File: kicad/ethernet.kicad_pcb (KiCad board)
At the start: 2 copper layers, 2 parts, among them J1 RJ45_Abracon_ARJP11A-MASA-B-A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, U1 MSP432E401Y

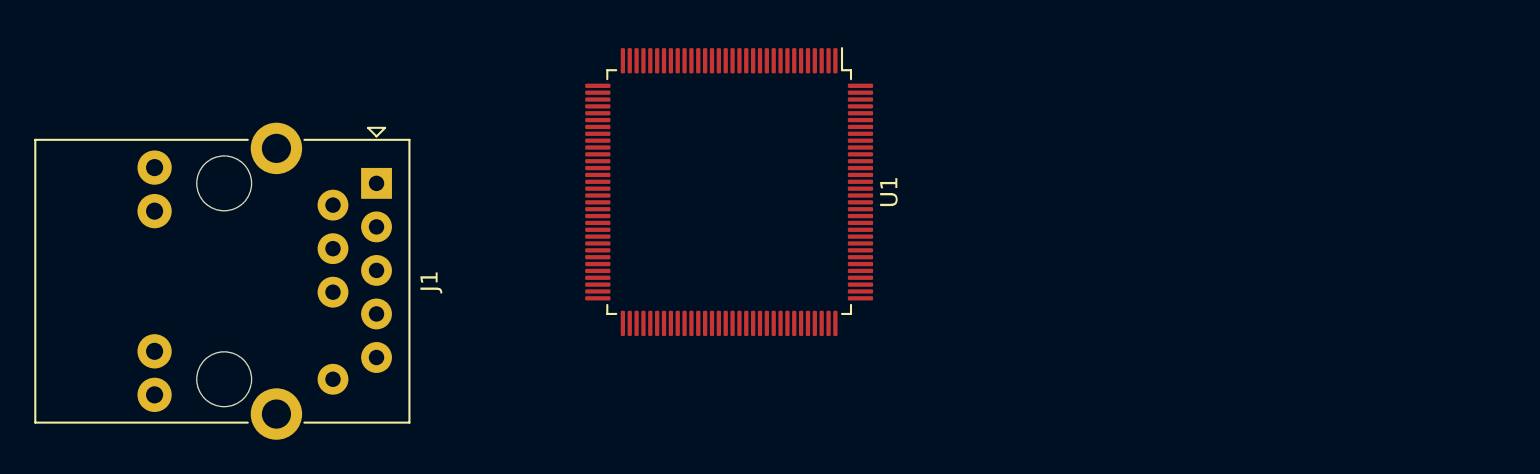
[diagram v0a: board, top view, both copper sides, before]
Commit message: working on ethernet board
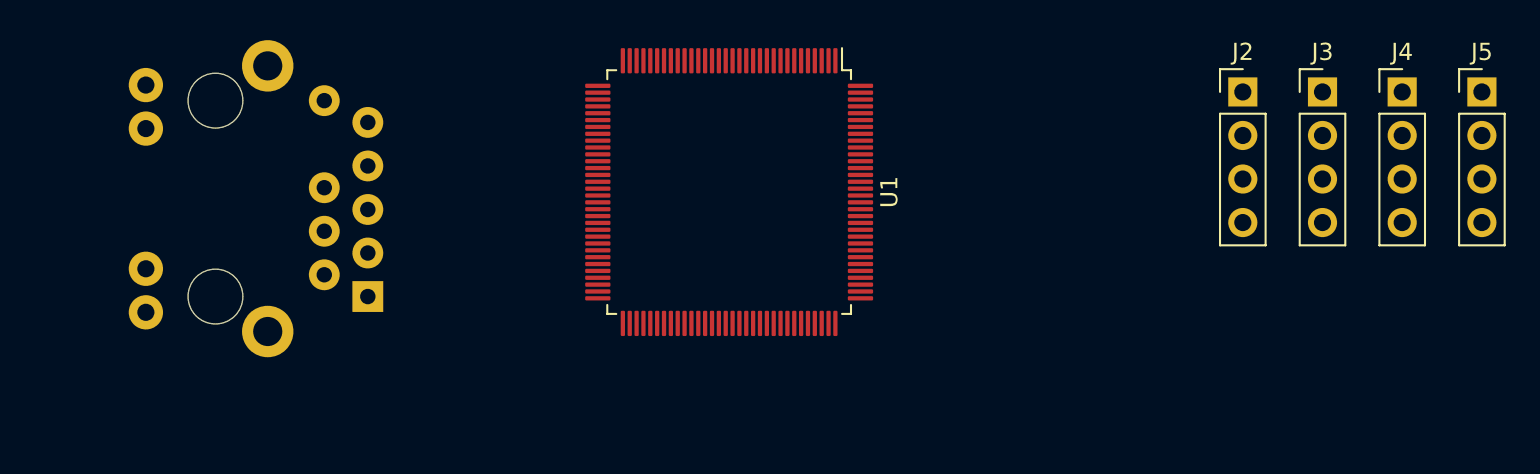
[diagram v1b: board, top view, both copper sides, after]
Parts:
- added J2: Conn_01x04_Male, Connector_PinHeader_2.54mm:PinHeader_1x04_P2.54mm_Vertical, F.Cu at (91.7, 32.0)
- added J3: Conn_01x04_Male, Connector_PinHeader_2.54mm:PinHeader_1x04_P2.54mm_Vertical, F.Cu at (96.3, 32.0)
- added J4: Conn_01x04_Male, Connector_PinHeader_2.54mm:PinHeader_1x04_P2.54mm_Vertical, F.Cu at (101.0, 32.0)
- added J5: Conn_01x04_Male, Connector_PinHeader_2.54mm:PinHeader_1x04_P2.54mm_Vertical, F.Cu at (105.6, 32.0)
- J1: moved to B.Cu
- moved J1 6.62 mm to (40.6, 43.9), turned to 90 degrees
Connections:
- J1 pad 7: Net-(J1-Pad7) -> GND
- U1 pad 10: Net-(U1-Pad10) -> GND
- U1 pad 114: Net-(U1-Pad114) -> GND
- U1 pad 17: Net-(U1-Pad114) -> GND
- U1 pad 48: Net-(U1-Pad114) -> GND
- U1 pad 55: Net-(U1-Pad114) -> GND
- U1 pad 58: Net-(U1-Pad114) -> GND
- U1 pad 80: Net-(U1-Pad114) -> GND

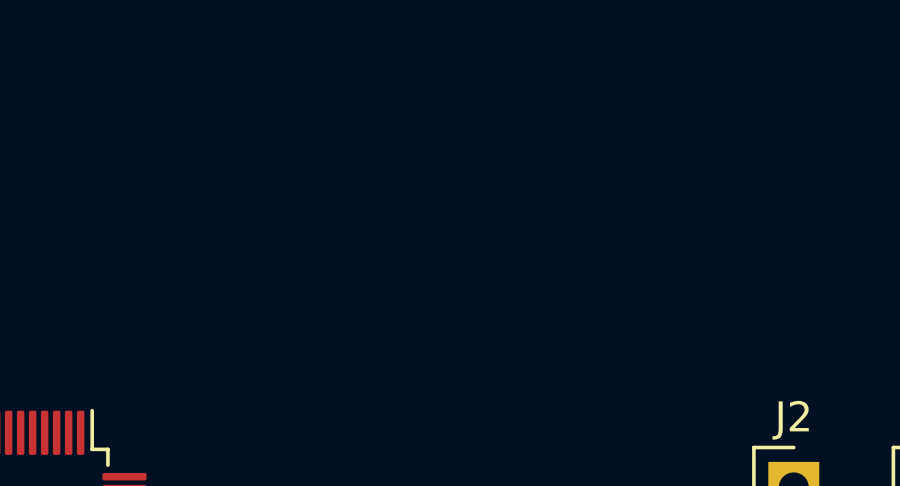
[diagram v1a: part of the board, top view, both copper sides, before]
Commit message: add QSPI flash to ethernet board
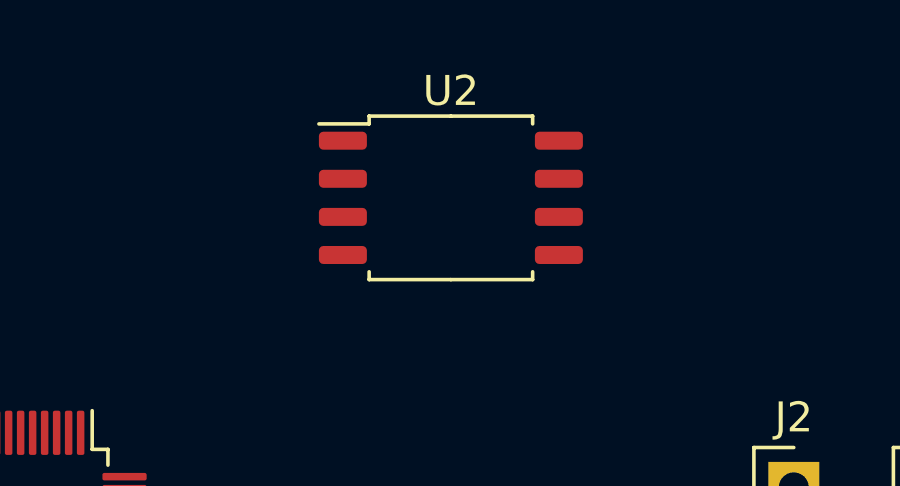
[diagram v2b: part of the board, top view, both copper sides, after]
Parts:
- added U2: W25Q32JVSS, Package_SO:SOIC-8_5.23x5.23mm_P1.27mm, F.Cu at (80.3, 22.4)
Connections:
- J1 pad 4: Net-(J1-Pad4) -> +3V3
- J1 pad 5: Net-(J1-Pad5) -> +3V3

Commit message: updating board
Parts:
- removed J2, J3, J4, J5: Conn_01x04_Male, Connector_PinHeader_2.54mm:PinHeader_1x04_P2.54mm_Vertical
- removed U2: W25Q32JVSS, Package_SO:SOIC-8_5.23x5.23mm_P1.27mm
- added R1: 49.9, Resistor_SMD:R_0805_2012Metric, F.Cu at (45.5, 32.5)
- added R2: 49.9, Resistor_SMD:R_0805_2012Metric, F.Cu at (49.0, 30.5)
- added R3: 49.9, Resistor_SMD:R_0805_2012Metric, F.Cu at (45.5, 29.0)
- added R4: 49.9, Resistor_SMD:R_0805_2012Metric, F.Cu at (49.0, 27.0)
- J1: moved to F.Cu
- U1: value MSP432E401Y -> TM4C1294NCPDTI3; footprint Package_QFP:LQFP-128_14x14mm_P0.4mm -> Package_QFP:TQFP-128_14x14mm_P0.4mm
- moved J1 17.2 mm to (39.0, 26.8), turned to -90 degrees
- moved U1 9.40 mm to (66.5, 29.8)
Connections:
- J1 pad 10: Net-(J1-Pad10) -> unconnected-(J1-Pad10)
- J1 pad 11: Net-(J1-Pad11) -> unconnected-(J1-Pad11)
- J1 pad 12: Net-(J1-Pad12) -> unconnected-(J1-Pad12)
- J1 pad 13: Net-(J1-Pad13) -> unconnected-(J1-Pad13)
- J1 pad 14: Net-(J1-Pad14) -> unconnected-(J1-Pad14)
- J1 pad 15: Net-(J1-Pad15) -> unconnected-(J1-Pad15)
- J1 pad 9: Net-(J1-Pad9) -> unconnected-(J1-Pad9)
- U1 pad 1: Net-(U1-Pad1) -> unconnected-(U1-Pad1)
- U1 pad 100: Net-(U1-Pad100) -> unconnected-(U1-Pad100)
- U1 pad 101: Net-(U1-Pad101) -> unconnected-(U1-Pad101)
- U1 pad 102: Net-(U1-Pad102) -> unconnected-(U1-Pad102)
- U1 pad 103: Net-(U1-Pad103) -> unconnected-(U1-Pad103)
- U1 pad 104: Net-(U1-Pad104) -> unconnected-(U1-Pad104)
- U1 pad 105: Net-(U1-Pad105) -> unconnected-(U1-Pad105)
- U1 pad 106: Net-(U1-Pad106) -> unconnected-(U1-Pad106)
- U1 pad 107: Net-(U1-Pad107) -> unconnected-(U1-Pad107)
- U1 pad 108: Net-(U1-Pad108) -> unconnected-(U1-Pad108)
- U1 pad 109: Net-(U1-Pad109) -> unconnected-(U1-Pad109)
- U1 pad 11: Net-(U1-Pad11) -> unconnected-(U1-Pad11)
- U1 pad 110: Net-(U1-Pad110) -> unconnected-(U1-Pad110)
- U1 pad 111: Net-(U1-Pad111) -> unconnected-(U1-Pad111)
- U1 pad 112: Net-(U1-Pad112) -> unconnected-(U1-Pad112)
- U1 pad 113: Net-(U1-Pad113) -> unconnected-(U1-Pad113)
- U1 pad 115: Net-(U1-Pad115) -> unconnected-(U1-Pad115)
- U1 pad 116: Net-(U1-Pad116) -> unconnected-(U1-Pad116)
- U1 pad 117: Net-(U1-Pad117) -> unconnected-(U1-Pad117)
- U1 pad 118: Net-(U1-Pad118) -> unconnected-(U1-Pad118)
- U1 pad 119: Net-(U1-Pad119) -> unconnected-(U1-Pad119)
- U1 pad 12: Net-(U1-Pad12) -> unconnected-(U1-Pad12)
- U1 pad 120: Net-(U1-Pad120) -> unconnected-(U1-Pad120)
- U1 pad 121: Net-(U1-Pad121) -> unconnected-(U1-Pad121)
- U1 pad 122: Net-(U1-Pad122) -> unconnected-(U1-Pad122)
- U1 pad 123: Net-(U1-Pad123) -> unconnected-(U1-Pad123)
- U1 pad 124: Net-(U1-Pad124) -> unconnected-(U1-Pad124)
- U1 pad 125: Net-(U1-Pad125) -> unconnected-(U1-Pad125)
- U1 pad 126: Net-(U1-Pad126) -> unconnected-(U1-Pad126)
- U1 pad 127: Net-(U1-Pad127) -> unconnected-(U1-Pad127)
- U1 pad 128: Net-(U1-Pad128) -> unconnected-(U1-Pad128)
- U1 pad 13: Net-(U1-Pad13) -> unconnected-(U1-Pad13)
- U1 pad 14: Net-(U1-Pad14) -> unconnected-(U1-Pad14)
- U1 pad 15: Net-(U1-Pad15) -> unconnected-(U1-Pad15)
- U1 pad 16: Net-(U1-Pad16) -> unconnected-(U1-Pad16)
- U1 pad 18: Net-(U1-Pad18) -> unconnected-(U1-Pad18)
- U1 pad 19: Net-(U1-Pad19) -> unconnected-(U1-Pad19)
- U1 pad 2: Net-(U1-Pad2) -> unconnected-(U1-Pad2)
- U1 pad 20: Net-(U1-Pad20) -> unconnected-(U1-Pad20)
- U1 pad 21: Net-(U1-Pad21) -> unconnected-(U1-Pad21)
- U1 pad 22: Net-(U1-Pad22) -> unconnected-(U1-Pad22)
- U1 pad 23: Net-(U1-Pad23) -> unconnected-(U1-Pad23)
- U1 pad 24: Net-(U1-Pad24) -> unconnected-(U1-Pad24)
- U1 pad 25: Net-(U1-Pad25) -> unconnected-(U1-Pad25)
- U1 pad 26: Net-(U1-Pad26) -> unconnected-(U1-Pad26)
- U1 pad 27: Net-(U1-Pad27) -> unconnected-(U1-Pad27)
- U1 pad 28: Net-(U1-Pad28) -> unconnected-(U1-Pad28)
- U1 pad 29: Net-(U1-Pad29) -> unconnected-(U1-Pad29)
- U1 pad 3: Net-(U1-Pad3) -> unconnected-(U1-Pad3)
- U1 pad 30: Net-(U1-Pad30) -> unconnected-(U1-Pad30)
- U1 pad 31: Net-(U1-Pad31) -> unconnected-(U1-Pad31)
- U1 pad 32: Net-(U1-Pad32) -> unconnected-(U1-Pad32)
- U1 pad 33: Net-(U1-Pad33) -> unconnected-(U1-Pad33)
- U1 pad 34: Net-(U1-Pad34) -> unconnected-(U1-Pad34)
- U1 pad 35: Net-(U1-Pad35) -> unconnected-(U1-Pad35)
- U1 pad 36: Net-(U1-Pad36) -> unconnected-(U1-Pad36)
- U1 pad 37: Net-(U1-Pad37) -> unconnected-(U1-Pad37)
- U1 pad 38: Net-(U1-Pad38) -> unconnected-(U1-Pad38)
- U1 pad 39: Net-(U1-Pad39) -> unconnected-(U1-Pad39)
- U1 pad 4: Net-(U1-Pad4) -> unconnected-(U1-Pad4)
- U1 pad 40: Net-(U1-Pad40) -> unconnected-(U1-Pad40)
- U1 pad 41: Net-(U1-Pad41) -> unconnected-(U1-Pad41)
- U1 pad 42: Net-(U1-Pad42) -> unconnected-(U1-Pad42)
- U1 pad 43: Net-(U1-Pad43) -> unconnected-(U1-Pad43)
- U1 pad 44: Net-(U1-Pad44) -> unconnected-(U1-Pad44)
- U1 pad 45: Net-(U1-Pad45) -> unconnected-(U1-Pad45)
- U1 pad 46: Net-(U1-Pad46) -> unconnected-(U1-Pad46)
- U1 pad 47: Net-(U1-Pad47) -> unconnected-(U1-Pad47)
- U1 pad 49: Net-(U1-Pad49) -> unconnected-(U1-Pad49)
- U1 pad 5: Net-(U1-Pad5) -> unconnected-(U1-Pad5)
- U1 pad 50: Net-(U1-Pad50) -> unconnected-(U1-Pad50)
- U1 pad 51: Net-(U1-Pad51) -> unconnected-(U1-Pad51)
- U1 pad 52: Net-(U1-Pad52) -> unconnected-(U1-Pad52)
- U1 pad 59: Net-(U1-Pad59) -> unconnected-(U1-Pad59)
- U1 pad 6: Net-(U1-Pad6) -> unconnected-(U1-Pad6)
- U1 pad 60: Net-(U1-Pad60) -> unconnected-(U1-Pad60)
- U1 pad 61: Net-(U1-Pad61) -> unconnected-(U1-Pad61)
- U1 pad 62: Net-(U1-Pad62) -> unconnected-(U1-Pad62)
- U1 pad 63: Net-(U1-Pad63) -> unconnected-(U1-Pad63)
- U1 pad 64: Net-(U1-Pad64) -> unconnected-(U1-Pad64)
- U1 pad 65: Net-(U1-Pad65) -> unconnected-(U1-Pad65)
- U1 pad 66: Net-(U1-Pad66) -> unconnected-(U1-Pad66)
- U1 pad 67: Net-(U1-Pad67) -> unconnected-(U1-Pad67)
- U1 pad 68: Net-(U1-Pad68) -> unconnected-(U1-Pad68)
- U1 pad 69: Net-(U1-Pad69) -> unconnected-(U1-Pad69)
- U1 pad 7: Net-(U1-Pad7) -> unconnected-(U1-Pad7)
- U1 pad 70: Net-(U1-Pad70) -> unconnected-(U1-Pad70)
- U1 pad 71: Net-(U1-Pad71) -> unconnected-(U1-Pad71)
- U1 pad 72: Net-(U1-Pad72) -> unconnected-(U1-Pad72)
- U1 pad 73: Net-(U1-Pad73) -> unconnected-(U1-Pad73)
- U1 pad 74: Net-(U1-Pad74) -> unconnected-(U1-Pad74)
- U1 pad 75: Net-(U1-Pad75) -> unconnected-(U1-Pad75)
- U1 pad 76: Net-(U1-Pad76) -> unconnected-(U1-Pad76)
- U1 pad 77: Net-(U1-Pad77) -> unconnected-(U1-Pad77)
- U1 pad 78: Net-(U1-Pad78) -> unconnected-(U1-Pad78)
- U1 pad 79: Net-(U1-Pad79) -> unconnected-(U1-Pad79)
- U1 pad 8: Net-(U1-Pad8) -> unconnected-(U1-Pad8)
- U1 pad 81: Net-(U1-Pad81) -> unconnected-(U1-Pad81)
- U1 pad 82: Net-(U1-Pad82) -> unconnected-(U1-Pad82)
- U1 pad 83: Net-(U1-Pad83) -> unconnected-(U1-Pad83)
- U1 pad 84: Net-(U1-Pad84) -> unconnected-(U1-Pad84)
- U1 pad 85: Net-(U1-Pad85) -> unconnected-(U1-Pad85)
- U1 pad 86: Net-(U1-Pad86) -> unconnected-(U1-Pad86)
- U1 pad 87: Net-(U1-Pad87) -> unconnected-(U1-Pad87)
- U1 pad 88: Net-(U1-Pad88) -> unconnected-(U1-Pad88)
- U1 pad 89: Net-(U1-Pad89) -> unconnected-(U1-Pad89)
- U1 pad 9: Net-(U1-Pad9) -> unconnected-(U1-Pad9)
- U1 pad 90: Net-(U1-Pad90) -> unconnected-(U1-Pad90)
- U1 pad 91: Net-(U1-Pad91) -> unconnected-(U1-Pad91)
- U1 pad 92: Net-(U1-Pad92) -> unconnected-(U1-Pad92)
- U1 pad 93: Net-(U1-Pad93) -> unconnected-(U1-Pad93)
- U1 pad 94: Net-(U1-Pad94) -> unconnected-(U1-Pad94)
- U1 pad 95: Net-(U1-Pad95) -> unconnected-(U1-Pad95)
- U1 pad 96: Net-(U1-Pad96) -> unconnected-(U1-Pad96)
- U1 pad 97: Net-(U1-Pad97) -> unconnected-(U1-Pad97)
- U1 pad 98: Net-(U1-Pad98) -> unconnected-(U1-Pad98)
- U1 pad 99: Net-(U1-Pad99) -> unconnected-(U1-Pad99)
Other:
- net class Default removed

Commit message: board layout
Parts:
- added C1: 100n, Capacitor_SMD:C_0805_2012Metric, F.Cu at (71.0, 41.0)
- added C10: 100n, Capacitor_SMD:C_0805_2012Metric, F.Cu at (80.5, 61.0)
- added C11: 100n, Capacitor_SMD:C_0805_2012Metric, F.Cu at (80.5, 64.0)
- added C12: 100n, Capacitor_SMD:C_0805_2012Metric, F.Cu at (76.0, 61.0)
- added C13: 4.7n, Capacitor_SMD:C_0805_2012Metric, F.Cu at (31.8, 19.8)
- added C14: 10n, Capacitor_SMD:C_0805_2012Metric, F.Cu at (53.8, 55.5)
- added C2: 100n, Capacitor_SMD:C_0805_2012Metric, F.Cu at (70.0, 44.0)
- added C3: 100n, Capacitor_SMD:C_0805_2012Metric, F.Cu at (67.0, 43.0)
- added C4: 100n, Capacitor_SMD:C_0805_2012Metric, F.Cu at (63.5, 40.0)
- added C5: 100n, Capacitor_SMD:C_0805_2012Metric, F.Cu at (55.0, 37.2)
- added C6: 100n, Capacitor_SMD:C_0805_2012Metric, F.Cu at (84.9, 64.0)
- added C7: 100n, Capacitor_SMD:C_0805_2012Metric, F.Cu at (52.5, 37.2)
- added C8: 100n, Capacitor_SMD:C_0805_2012Metric, F.Cu at (76.0, 64.0)
- added C9: 100n, Capacitor_SMD:C_0805_2012Metric, F.Cu at (84.9, 61.0)
- added J2: Conn_Coaxial, Connector_Coaxial:SMA_Molex_73251-2120_EdgeMount_Horizontal, F.Cu at (25.5, 54.5)
- added L1: 27n, Inductor_SMD:L_0805_2012Metric, F.Cu at (50.8, 54.5)
- added R10: 10, Resistor_SMD:R_0805_2012Metric, F.Cu at (56.0, 53.5)
- added R5: 10k, Resistor_SMD:R_0805_2012Metric, F.Cu at (71.0, 38.5)
- added R6: 10k, Resistor_SMD:R_0805_2012Metric, F.Cu at (72.5, 44.0)
- added R7: 10k, Resistor_SMD:R_0805_2012Metric, F.Cu at (67.0, 45.5)
- added R8: 1M, Resistor_SMD:R_0805_2012Metric, F.Cu at (34.2, 19.8)
- added R9: 4.87k, Resistor_SMD:R_0805_2012Metric, F.Cu at (52.8, 32.8)
- added U2: MAX-8Q, RF_GPS:ublox_MAX, F.Cu at (56.0, 45.2)
- added X1: TXEAADSANF-25.000000, Oscillator:Oscillator_SMD_SeikoEpson_SG8002CE-4Pin_3.2x2.5mm, F.Cu at (67.0, 40.0)
- U1: value TM4C1294NCPDTI3 -> MSP432E401Y; footprint Package_QFP:TQFP-128_14x14mm_P0.4mm -> Package_QFP:LQFP-128_14x14mm_P0.4mm
- moved R4 7.38 mm to (45.5, 33.5), turned to 90 degrees
- moved R3 5.03 mm to (47.8, 33.5)
- moved R1 5.00 mm to (45.5, 27.5)
- moved R2 3.25 mm to (47.8, 27.5), turned to -90 degrees
- moved U1 2.30 mm to (65.0, 28.0)
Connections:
- J1 pad 15: unconnected-(J1-Pad15) -> Net-(J1-Pad15)
- U1 pad 101: unconnected-(U1-Pad101) -> +3V3
- U1 pad 113: unconnected-(U1-Pad113) -> +3V3
- U1 pad 122: unconnected-(U1-Pad122) -> +3V3
- U1 pad 16: unconnected-(U1-Pad16) -> +3V3
- U1 pad 26: unconnected-(U1-Pad26) -> +3V3
- U1 pad 28: unconnected-(U1-Pad28) -> +3V3
- U1 pad 39: unconnected-(U1-Pad39) -> +3V3
- U1 pad 47: unconnected-(U1-Pad47) -> +3V3
- U1 pad 49: unconnected-(U1-Pad49) -> uPPS
- U1 pad 51: unconnected-(U1-Pad51) -> +3V3
- U1 pad 52: unconnected-(U1-Pad52) -> +3V3
- U1 pad 59: unconnected-(U1-Pad59) -> Net-(U1-Pad59)
- U1 pad 69: unconnected-(U1-Pad69) -> +3V3
- U1 pad 7: unconnected-(U1-Pad7) -> +3V3
- U1 pad 71: unconnected-(U1-Pad71) -> gPPS
- U1 pad 72: unconnected-(U1-Pad72) -> uPPS
- U1 pad 79: unconnected-(U1-Pad79) -> +3V3
- U1 pad 88: unconnected-(U1-Pad88) -> Net-(U1-Pad88)
- U1 pad 90: unconnected-(U1-Pad90) -> +3V3
- U1 pad 93: unconnected-(U1-Pad93) -> Net-(U1-Pad93)
- U1 pad 95: unconnected-(U1-Pad95) -> gTX
- U1 pad 96: unconnected-(U1-Pad96) -> gRX
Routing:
- net gRX: track 0.00 -> 37.7 mm
- net gTX: track 0.00 -> 36.3 mm
- net Net-(J1-Pad6): track 0.00 -> 26.2 mm
- net Net-(J1-Pad2): track 0.00 -> 26.2 mm, vias 0 -> 1
- net Net-(J1-Pad1): track 0.00 -> 22.1 mm, vias 0 -> 1
- net Net-(J1-Pad15): track 0.00 -> 22.0 mm
- net Net-(J1-Pad3): track 0.00 -> 19.5 mm
- net GND: track 0.00 -> 12.4 mm, vias 0 -> 24
- net uPPS: track 0.00 -> 10.2 mm
- net gPPS: track 0.00 -> 7.44 mm
- net Net-(U2-Pad11): track 0.00 -> 5.73 mm
- net Net-(C2-Pad1): track 0.00 -> 4.83 mm
- net Net-(C1-Pad1): track 0.00 -> 4.83 mm
- net Net-(C3-Pad1): track 0.00 -> 4.67 mm
- net Net-(C14-Pad1): track 0.00 -> 4.27 mm
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- added copper zone on F.Cu, net +3V3
- added copper zone on B.Cu, net GND
- added copper zone on F.Cu, net GND
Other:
- board outline added: 67 x 57 mm

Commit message: board layout
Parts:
- added C15: 100n, Capacitor_SMD:C_0805_2012Metric, F.Cu at (66.0, 46.0)
- added C16: 100n, Capacitor_SMD:C_0805_2012Metric, F.Cu at (77.8, 35.0)
- added C17: 2.7u, Capacitor_SMD:C_0805_2012Metric, F.Cu at (77.8, 32.8)
- added J3: MSP-FET, Connector_PinHeader_2.54mm:PinHeader_2x07_P2.54mm_Vertical, F.Cu at (86.2, 44.1)
- added R11: 10k, Resistor_SMD:R_0805_2012Metric, F.Cu at (61.0, 63.0)
- added R12: 10k, Resistor_SMD:R_0805_2012Metric, F.Cu at (86.0, 63.0)
- added R13: 330, Resistor_SMD:R_0805_2012Metric, F.Cu at (25.0, 29.5)
- added R14: 330, Resistor_SMD:R_0805_2012Metric, F.Cu at (27.2, 29.5)
- added SW1: KSC701, Button_Switch_SMD:SW_Push_1P1T_NO_CK_KSC7xxJ, F.Cu at (68.0, 65.0)
- added SW2: KSC701, Button_Switch_SMD:SW_Push_1P1T_NO_CK_KSC7xxJ, F.Cu at (79.0, 65.0)
- moved C12 48.8 mm to (42.5, 25.5)
- moved C6 42.5 mm to (52.8, 36.2), turned to 180 degrees
- moved C11 42.2 mm to (52.8, 32.2), turned to 180 degrees
- moved C10 32.9 mm to (77.8, 28.2)
- moved C9 23.9 mm to (77.8, 38.2)
- moved C8 20.3 mm to (75.8, 43.8)
- moved C1 9.00 mm to (71.0, 50.0)
- moved C2 9.00 mm to (70.0, 53.0)
- moved C3 9.00 mm to (67.0, 52.0)
- moved C4 9.00 mm to (63.5, 49.0)
- moved R5 9.00 mm to (71.0, 47.5)
- moved R6 9.00 mm to (72.5, 53.0)
- moved R7 9.00 mm to (67.0, 54.5)
- moved X1 9.00 mm to (67.0, 49.0)
- moved C13 8.01 mm to (31.7, 27.8)
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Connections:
- J1 pad 11: unconnected-(J1-Pad11) -> Net-(J1-Pad11)
- J1 pad 12: unconnected-(J1-Pad12) -> GND
- J1 pad 13: unconnected-(J1-Pad13) -> Net-(J1-Pad13)
- J1 pad 14: unconnected-(J1-Pad14) -> GND
- U1 pad 100: unconnected-(U1-Pad100) -> Net-(U1-Pad100)
- U1 pad 102: unconnected-(U1-Pad102) -> +3V3
- U1 pad 103: unconnected-(U1-Pad103) -> +3V3
- U1 pad 104: unconnected-(U1-Pad104) -> +3V3
- U1 pad 105: unconnected-(U1-Pad105) -> +3V3
- U1 pad 106: unconnected-(U1-Pad106) -> +3V3
- U1 pad 107: unconnected-(U1-Pad107) -> +3V3
- U1 pad 108: unconnected-(U1-Pad108) -> +3V3
- U1 pad 109: unconnected-(U1-Pad109) -> +3V3
- U1 pad 110: unconnected-(U1-Pad110) -> +3V3
- U1 pad 111: unconnected-(U1-Pad111) -> +3V3
- U1 pad 112: unconnected-(U1-Pad112) -> +3V3
- U1 pad 115: unconnected-(U1-Pad115) -> Net-(U1-Pad115)
- U1 pad 42: unconnected-(U1-Pad42) -> ETH_LED0
- U1 pad 43: unconnected-(U1-Pad43) -> +3V3
- U1 pad 44: unconnected-(U1-Pad44) -> +3V3
- U1 pad 45: unconnected-(U1-Pad45) -> +3V3
- U1 pad 46: unconnected-(U1-Pad46) -> ETH_LED1
- U1 pad 50: unconnected-(U1-Pad50) -> +3V3
- U1 pad 60: unconnected-(U1-Pad60) -> +3V3
- U1 pad 61: unconnected-(U1-Pad61) -> +3V3
- U1 pad 62: unconnected-(U1-Pad62) -> +3V3
- U1 pad 63: unconnected-(U1-Pad63) -> +3V3
- U1 pad 64: unconnected-(U1-Pad64) -> ~{WAKE}
- U1 pad 68: unconnected-(U1-Pad68) -> +3V3
- U1 pad 70: unconnected-(U1-Pad70) -> ~{RST}
- U1 pad 73: unconnected-(U1-Pad73) -> Net-(U1-Pad73)
- U1 pad 74: unconnected-(U1-Pad74) -> Net-(U1-Pad74)
- U1 pad 75: unconnected-(U1-Pad75) -> +3V3
- U1 pad 76: unconnected-(U1-Pad76) -> +3V3
- U1 pad 77: unconnected-(U1-Pad77) -> +3V3
- U1 pad 78: unconnected-(U1-Pad78) -> +3V3
- U1 pad 8: unconnected-(U1-Pad8) -> +3V3
- U1 pad 81: unconnected-(U1-Pad81) -> +3V3
- U1 pad 82: unconnected-(U1-Pad82) -> +3V3
- U1 pad 83: unconnected-(U1-Pad83) -> +3V3
- U1 pad 84: unconnected-(U1-Pad84) -> +3V3
- U1 pad 85: unconnected-(U1-Pad85) -> +3V3
- U1 pad 86: unconnected-(U1-Pad86) -> +3V3
- U1 pad 87: unconnected-(U1-Pad87) -> Net-(U1-Pad115)
- U1 pad 9: unconnected-(U1-Pad9) -> +3V3
- U1 pad 91: unconnected-(U1-Pad91) -> +3V3
- U1 pad 92: unconnected-(U1-Pad92) -> +3V3
- U1 pad 94: unconnected-(U1-Pad94) -> +3V3
- U1 pad 97: unconnected-(U1-Pad97) -> Net-(U1-Pad97)
- U1 pad 98: unconnected-(U1-Pad98) -> Net-(U1-Pad98)
- U1 pad 99: unconnected-(U1-Pad99) -> Net-(U1-Pad99)
- U2 pad 5: unconnected-(U2-Pad5) -> Net-(U1-Pad73)
- U2 pad 9: unconnected-(U2-Pad9) -> Net-(U1-Pad74)
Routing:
- net ~{RST}: track 0.00 -> 82.0 mm, vias 0 -> 2
- net ~{WAKE}: track 0.00 -> 43.8 mm, vias 0 -> 2
- net ETH_LED0: track 0.00 -> 36.7 mm, vias 0 -> 2
- net ETH_LED1: track 0.00 -> 32.8 mm, vias 0 -> 2
- net Net-(U2-Pad11): track 5.73 -> 29.9 mm
- net Net-(U1-Pad115): track 0.00 -> 20.6 mm
- net Net-(U1-Pad74): track 0.00 -> 18.4 mm, vias 0 -> 2
- net Net-(U1-Pad97): track 0.00 -> 15.5 mm
- net Net-(U1-Pad100): track 0.00 -> 15.5 mm
- net Net-(J1-Pad13): track 0.00 -> 14.8 mm
- net Net-(U1-Pad99): track 0.00 -> 14.6 mm
- net Net-(U1-Pad98): track 0.00 -> 14.5 mm
- net Net-(U1-Pad73): track 0.00 -> 12.7 mm, vias 0 -> 2
- net Net-(J1-Pad11): track 0.00 -> 3.88 mm
- net GND: track 12.4 -> 15.5 mm, vias 24 -> 49
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
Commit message: board layout
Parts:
- added TR1: Wuerth_750315371, Transformer_SMD:Transformer_Wuerth_750315371, F.Cu at (51.3, 15.9)
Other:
- board text added: "RESET"
- board text added: "WAKE"
